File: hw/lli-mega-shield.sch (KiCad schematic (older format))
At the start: 31 parts

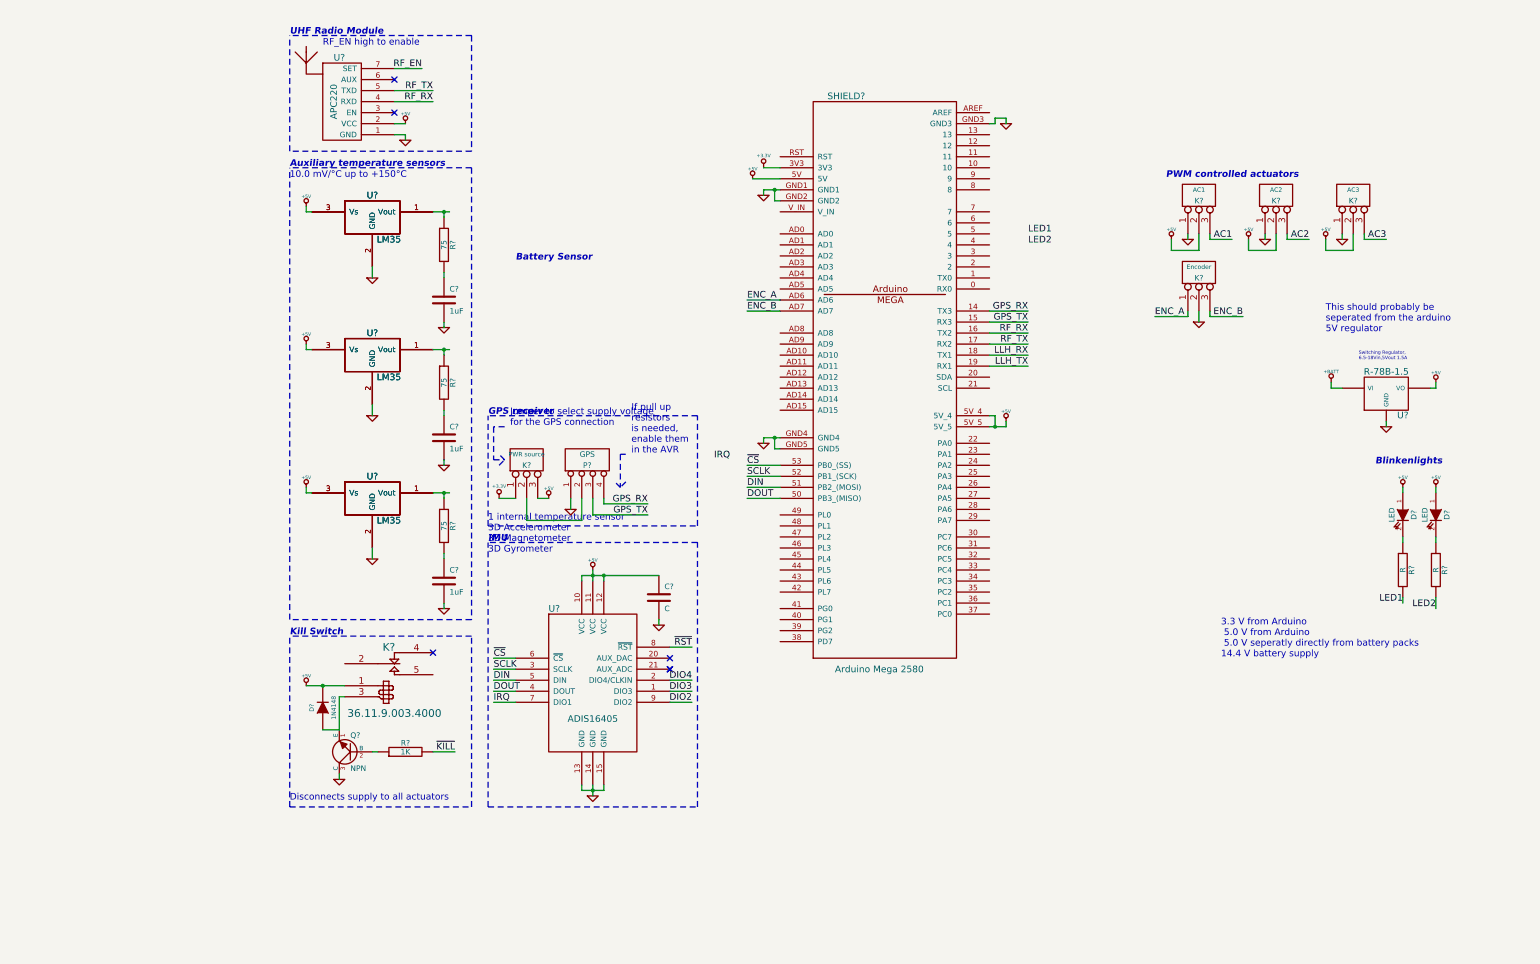
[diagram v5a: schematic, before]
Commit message: Some cleanup on schematic
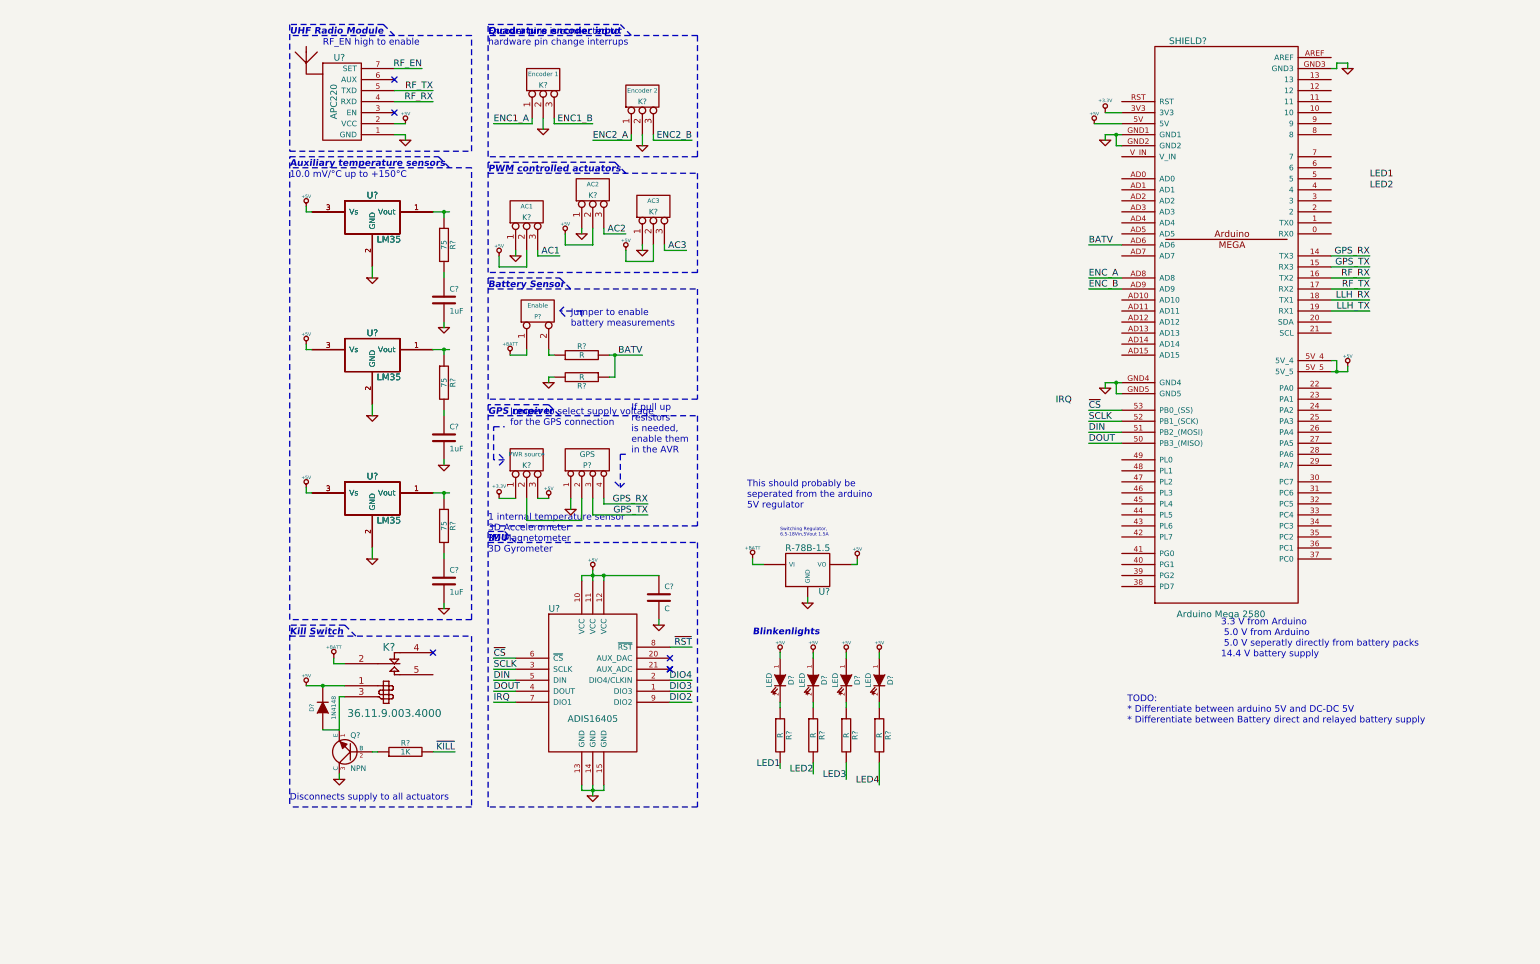
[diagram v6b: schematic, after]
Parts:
- added D? (x2): LED, symbol LED
- added K?: Encoder 1, symbol CONN_3
- added P?: Enable, symbol CONN_2
- added R? (x4): R, symbol R
- K?: value Encoder -> Encoder 2
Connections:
- net +5V: now also D?.1 (A), D?.1 (A)
- net +BATT: now also K?.2 (C1), P?.1 (P1)
- net ENC_A: now also SHIELD?.AD8; no longer K?.1 (P1), SHIELD?.AD6
- net ENC_B: now also SHIELD?.AD9; no longer K?.3 (P3), SHIELD?.AD7
- net GND: now also K?.2 (PM), R?.2
- new net: P?.2 (PM), R?.1
- new net: D?.2 (K), R?.1 (x2)
- new net BATV: R?.1, R?.2, SHIELD?.AD6
- new net ENC1_A: K?.1 (P1)
- new net ENC1_B: K?.3 (P3)
- new net ENC2_A: K?.1 (P1)
- new net ENC2_B: K?.3 (P3)
- new net LED3: R?.2
- new net LED4: R?.2
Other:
- note added: "Encoder pins is connected to\nhardware pin change interrups"
- note added: "Jumper to enable\nbattery measurements"
- note added: "Quadrature encoder input"
- note added: "TODO:\n* Differentiate between arduino 5V and DC-DC 5V\n* Differentiate between Battery direct and relayed battery supply"
- moved on the sheet: D?, K?, R?, SHIELD?, U?

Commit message: That must be hardware enough today
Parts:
- removed U? (x3): LM35, symbol LM35
- added K8: LLH UART, symbol CONN_3
- gave numbers to parts that had none: 36
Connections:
- net ENC_A is gone; now on net ENC1_A: SHIELD1.AD8
- net ENC_B is gone; now on net ENC1_B: SHIELD1.AD9
- net AC1: now also SHIELD1.AD0
- net AC2: now also SHIELD1.AD1
- net AC3: now also SHIELD1.AD2
- net BATV: now also SHIELD1.AD3; no longer SHIELD1.AD6
- net ENC2_A: now also SHIELD1.AD10
- net ENC2_B: now also SHIELD1.AD11
- net GND: now also K8.3 (P3)
- net LED1: now also SHIELD1.49 (PL0)
- net LED2: now also SHIELD1.48 (PL1)
- net LED3: now also SHIELD1.47 (PL2)
- net LED4: now also SHIELD1.46 (PL3)
- net LLH_RX: now also K8.2 (PM)
- net LLH_TX: now also K8.1 (P1)
- net ~KILL: now also SHIELD1.45 (PL4)
- net T1: now reaches SHIELD1.AD13
- net T1: now also R2.1, U2.1 (Vout)
- net T2: now reaches SHIELD1.AD14
- net T2: now also R3.1, U3.1 (Vout)
- net T3: now reaches SHIELD1.AD15
- net T3: now also R4.1, U4.1 (Vout)
- no-connect marks 6 -> 7
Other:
- note added: "Blinky"
- note added: "DC-DC converter 5V"
- note added: "Encoder"
- note added: "Maybe theese should be conn_3 molex\ninstead, so they can be placed remotely"
- note added: "Temperature"
- note added: "UART madness"
- moved on the sheet: C1, C2, C3, D2, D3, D4, D5, R10, R2, R3, R4, R7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
